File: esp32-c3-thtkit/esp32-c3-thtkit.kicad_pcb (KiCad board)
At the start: 4 copper layers, 17.9 x 24.5 mm, 28 parts, among them J1 PIN_GROUP_1, J2 PIN_GROUP_3, J3 PIN_GROUP_2, J4 UART, U1 MIC5219-3.3YM5, U2 ESP32-C3, Y1 32.768kHz ±20ppm CL12.5pF, Y2 40MHz ±10ppm CL8pF

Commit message: Draw pin layout on user layer
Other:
- board text added: "BOOT"
- board text added: "ESP32-C3-THTKIT"
- board text added: "GND"
- board text added: "GPIO10"
- board text added: "GPIO18"
- board text added: "GPIO19"
- board text added: "GPIO2"
- board text added: "GPIO3"
- board text added: "GPIO8"
- board text added: "MTCK"
- board text added: "MTDI"
- board text added: "MTDO"
- board text added: "MTMS"
- board text added: "RESET"
- board text added: "RX"
- board text added: "SPICLK"
- board text added: "SPICSO"
- board text added: "SPID"
- board text added: "SPIHD"
- board text added: "SPIQ"
- board text added: "SPIWP"
- board text added: "TX"
- board text added: "VIN"
- board text removed: "ESP32-C2-THTKIT"

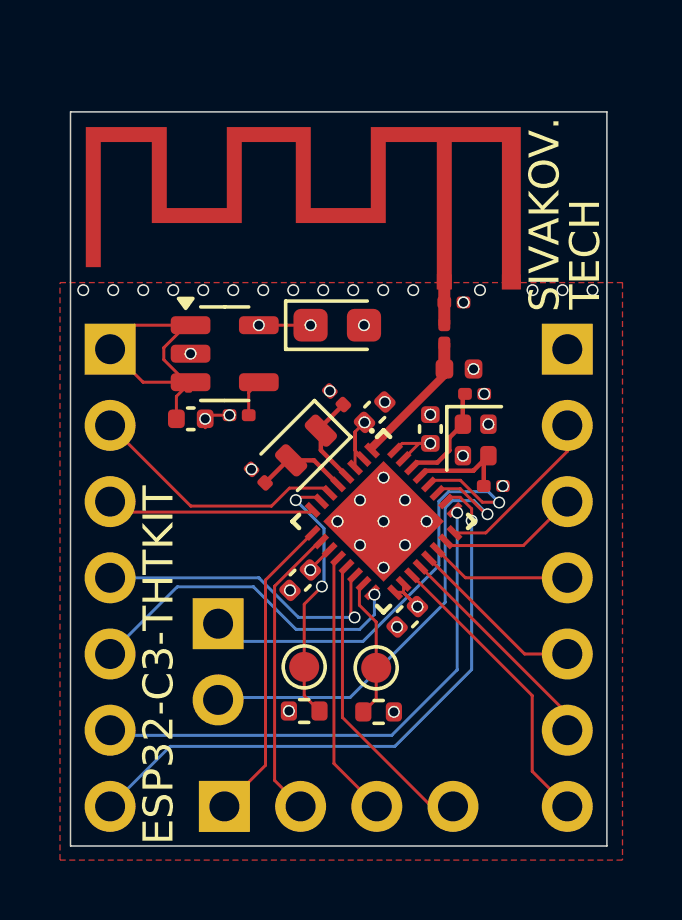
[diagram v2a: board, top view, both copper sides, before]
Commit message: Make devkits cheaper by using 0402 components instead of 0201
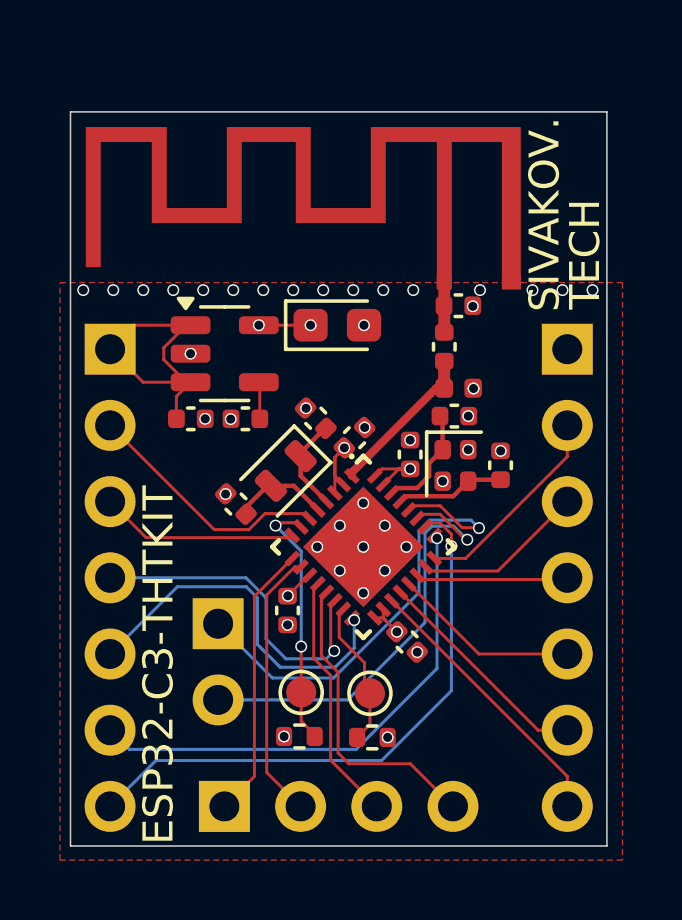
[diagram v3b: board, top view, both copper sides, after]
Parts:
- C10, C13: value 6p 6.3V C0G -> 15p 6.3V C0G; footprint Capacitor_SMD:C_0201_0603Metric -> Capacitor_SMD:C_0402_1005Metric
- C11, C12: value 15p 6.3V C0G -> 25p 6.3V C0G; footprint Capacitor_SMD:C_0201_0603Metric -> Capacitor_SMD:C_0402_1005Metric
- C2, C7, C9: footprint Capacitor_SMD:C_0201_0603Metric -> Capacitor_SMD:C_0402_1005Metric
- moved C12 1.19 mm to (189.6, 114.4)
- moved C5 1.09 mm to (191.3, 117.9), turned to 90 degrees
- moved C4 1.08 mm to (193.6, 112.2)
- moved C8 1.08 mm to (195.4, 112.7)
- moved U2 1.08 mm to (193.9, 115.8)
- moved Y2 1.08 mm to (196.9, 113.1)
- moved Y1 1.08 mm to (191.3, 113.3)
- moved C10 1.00 mm to (196.9, 111.5)
- moved C11 0.97 mm to (192.3, 111.5)
- moved R1 0.88 mm to (194.2, 122.2)
- moved TP1 0.88 mm to (194.1, 120.7)
- moved R2 0.86 mm to (191.7, 122.1)
- moved TP2 0.86 mm to (191.8, 120.7)
- moved C6 0.84 mm to (195.3, 119.0), turned to 135 degrees
- moved C13 0.73 mm to (198.4, 113.1), turned to -90 degrees
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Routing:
- net /GPIO18: track 17.8 -> 16.6 mm
- net /SPIQ: track 5.75 -> 6.88 mm
- net /MTMS: track 10.3 -> 9.21 mm
- net /GPIO19: track 20.4 -> 19.3 mm
- net /GPIO10: track 11.2 -> 12.3 mm
- net /U0RXD: track 15.9 -> 14.8 mm
- net /GPIO8: track 10.2 -> 11.3 mm
- net /SPID: track 4.71 -> 5.73 mm
- net /MTDO: track 9.99 -> 10.9 mm
- net GND: track 0.86 -> 0.00 mm
- net /MTDI: track 9.87 -> 9.04 mm
- net /RF: track 4.47 -> 5.27 mm
- net /U0TXD: track 15.8 -> 16.5 mm
- net /SPIHD: track 9.85 -> 9.27 mm
- net /MTCK: track 8.92 -> 8.34 mm
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
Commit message: Change microcontroller package from 4x4 to 5x5
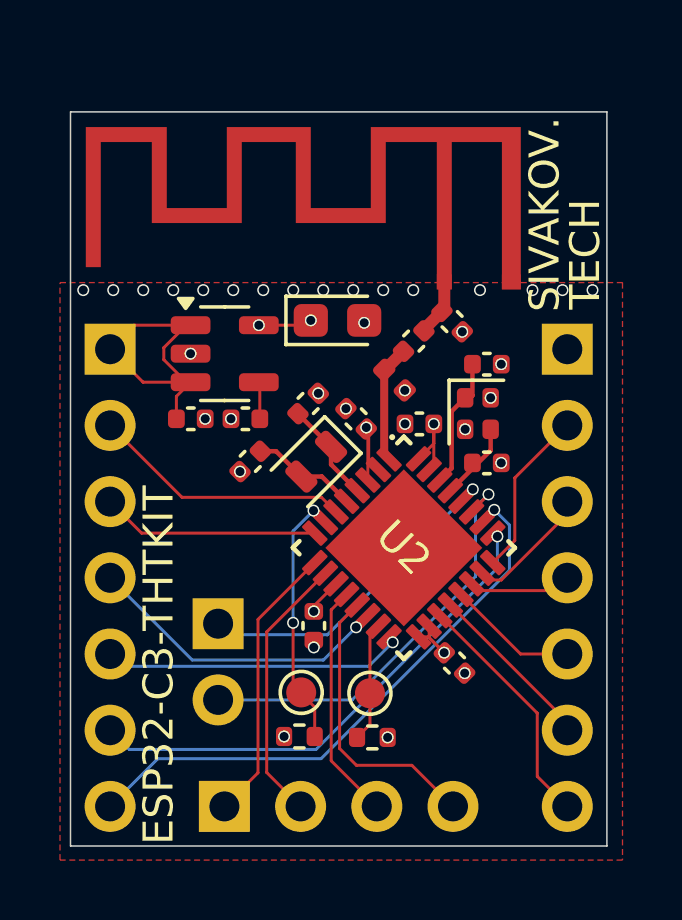
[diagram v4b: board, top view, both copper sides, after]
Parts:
- U2: footprint PCM_SKC_MCU_Espressif:TQFN_32_1EP_4x4mm_P0.4mm_EP2.4x2.4mm_Compact -> PCM_SKC_MCU_Espressif:VFQFN_32_1EP_5x5mm_P0.5mm_EP3.2x3.2mm_Compact
- moved L1 2.16 mm to (194.9, 110.2), turned to -45 degrees
- moved C10 2.04 mm to (198.0, 109.7)
- moved Y2 1.88 mm to (197.7, 111.4)
- moved C6 1.73 mm to (196.9, 119.7)
- moved C12 1.50 mm to (190.1, 113.0), turned to 45 degrees
- moved U2 1.35 mm to (195.2, 115.8)
- moved C8 1.07 mm to (195.7, 111.7), turned to 0 degrees
- moved Y1 1.06 mm to (192.3, 113.0)
- moved C7 1.04 mm to (195.5, 109.0), turned to -135 degrees
- moved C5 1.01 mm to (192.2, 118.4)
- moved C4 0.63 mm to (193.6, 111.5), turned to -45 degrees
- moved C9 0.57 mm to (196.8, 108.3), turned to 135 degrees
- moved C11 0.55 mm to (192.0, 111.0), turned to -135 degrees
- moved C13 0.46 mm to (198.0, 113.0), turned to 180 degrees
- moved C3 0.16 mm to (193.0, 108.3)
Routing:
- net /U0TXD: track 16.5 -> 11.2 mm
- net /GPIO10: track 12.3 -> 10.2 mm
- net /SPICS0: track 6.25 -> 4.37 mm
- net +3.3V: track 9.66 -> 11.5 mm
- net /SPIWP: track 8.02 -> 6.34 mm
- net /SPICLK: track 5.08 -> 3.46 mm
- net /SPID: track 5.73 -> 4.26 mm
- net /RF: track 5.27 -> 3.96 mm
- net /SPIQ: track 6.88 -> 5.60 mm
- net /XTAL_N: track 3.86 -> 2.60 mm
- net /SPIHD: track 9.27 -> 8.12 mm
- net /GPIO8: track 11.3 -> 10.3 mm
- net /U0RXD: track 14.8 -> 14.1 mm
- net /XTAL_P: track 3.55 -> 4.24 mm
- net /BOOT: track 4.93 -> 4.26 mm
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
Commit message: Unify schemas and fix esp32-c3 footprint
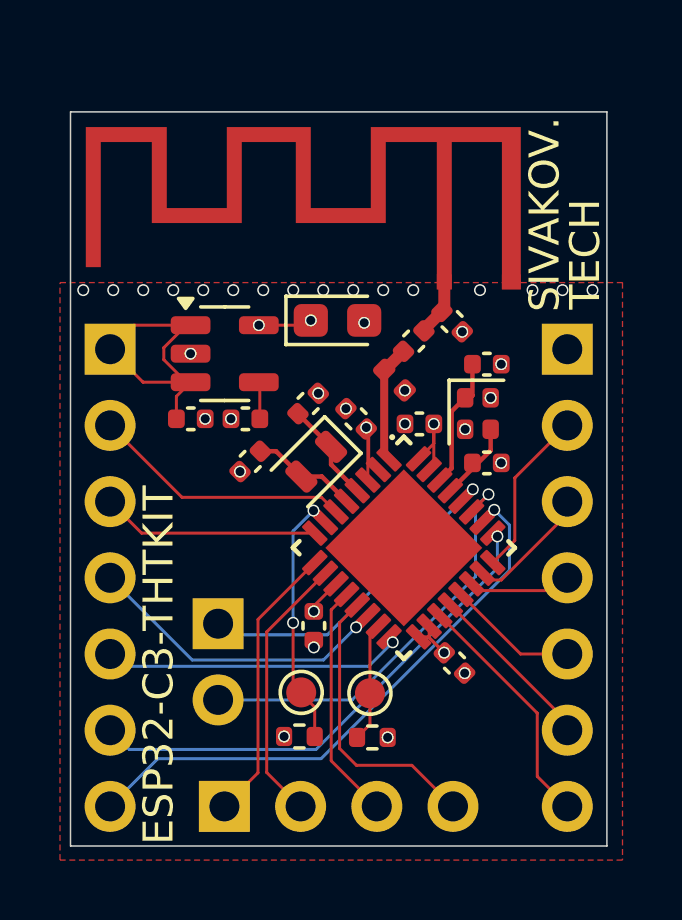
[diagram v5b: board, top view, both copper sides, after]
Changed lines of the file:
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@@
 			(unlocked yes)
 			(layer "F.SilkS")
+			(hide yes)
 			(effects
 				(font
@@
 			(unlocked yes)
 			(layer "F.Fab")
+			(hide yes)
 			(effects
 				(font
@@
 			)
 		)
-		(property "Datasheet" "https://cdn.jsdelivr.net/gh/sivakov512/kicad-library@master/datasheets/MCU/Espressif/Espressif_ESP32-C3.pdf"
+		(property "Datasheet" ""
 			(at -0.3 -6.699999 315)
 			(layer "F.Fab")
@@
 			)
 		)
-		(property "Description" "2.4 GHz Wi-Fi + BLE 5 LE SoC, 32-bit RISC-V MCU, 22 GPIO, QFN32"
+		(property "Description" ""
 			(at -0.3 -6.699999 315)
 			(layer "F.Fab")
@@
 		(sheetfile "esp32-c3-thtkit.kicad_sch")
 		(attr smd)
-		(fp_poly
-			(pts
-				(xy -1.9 -1.9) (xy 1.9 -1.9) (xy 1.9 1.9) (xy -1.9 1.9)
-			)
-			(stroke
-				(width 0.01)
-				(type solid)
-			)
-			(fill yes)
-			(layer "F.Mask")
-		)
 		(fp_line
 			(start -2.62 2.61)
@@
 			(at -2.445 -1.75 315)
 			(size 0.92 0.34)
-			(layers "F.Cu" "F.Paste")
+			(layers "F.Cu" "F.Mask" "F.Paste")
 			(roundrect_rratio 0.125)
 			(net 6 "/RF")
@@
 			(at -2.445001 -1.25 315)
 			(size 0.92 0.34)
-			(layers "F.Cu" "F.Paste")
+			(layers "F.Cu" "F.Mask" "F.Paste")
 			(roundrect_rratio 0.125)
 			(net 5 "+3.3V")
@@
 			(at -2.445 -0.75 315)
 			(size 0.92 0.34)
-			(layers "F.Cu" "F.Paste")
+			(layers "F.Cu" "F.Mask" "F.Paste")
 			(roundrect_rratio 0.125)
 			(net 5 "+3.3V")
@@
 			(at -2.445 -0.25 315)
 			(size 0.92 0.34)
-			(layers "F.Cu" "F.Paste")
+			(layers "F.Cu" "F.Mask" "F.Paste")
 			(roundrect_rratio 0.125)
 			(net 8 "/XTAL_32K_P")
@@
 			(at -2.445 0.25 315)
 			(size 0.92 0.34)
-			(layers "F.Cu" "F.Paste")
+			(layers "F.Cu" "F.Mask" "F.Paste")
 			(roundrect_rratio 0.125)
 			(net 9 "/XTAL_32K_N")
@@
 			(at -2.445 0.75 315)
 			(size 0.92 0.34)
-			(layers "F.Cu" "F.Paste")
+			(layers "F.Cu" "F.Mask" "F.Paste")
 			(roundrect_rratio 0.125)
 			(net 30 "/GPIO2")
@@
 			(at -2.445001 1.25 315)
 			(size 0.92 0.34)
-			(layers "F.Cu" "F.Paste")
+			(layers "F.Cu" "F.Mask" "F.Paste")
 			(roundrect_rratio 0.125)
 			(net 18 "/RESET")
@@
 			(at -2.445 1.75 315)
 			(size 0.92 0.34)
-			(layers "F.Cu" "F.Paste")
+			(layers "F.Cu" "F.Mask" "F.Paste")
 			(roundrect_rratio 0.125)
 			(net 22 "/GPIO3")
@@
 			(at -1.75 2.445 315)
 			(size 0.34 0.92)
-			(layers "F.Cu" "F.Paste")
+			(layers "F.Cu" "F.Mask" "F.Paste")
 			(roundrect_rratio 0.125)
 			(net 14 "/MTMS")
@@
 			(at -1.25 2.445001 315)
 			(size 0.34 0.92)
-			(layers "F.Cu" "F.Paste")
+			(layers "F.Cu" "F.Mask" "F.Paste")
 			(roundrect_rratio 0.125)
 			(net 13 "/MTDI")
@@
 			(at -0.75 2.445 315)
 			(size 0.34 0.92)
-			(layers "F.Cu" "F.Paste")
+			(layers "F.Cu" "F.Mask" "F.Paste")
 			(roundrect_rratio 0.125)
 			(net 5 "+3.3V")
@@
 			(at -0.25 2.445 315)
 			(size 0.34 0.92)
-			(layers "F.Cu" "F.Paste")
+			(layers "F.Cu" "F.Mask" "F.Paste")
 			(roundrect_rratio 0.125)
 			(net 12 "/MTCK")
@@
 			(at 0.25 2.445 315)
 			(size 0.34 0.92)
-			(layers "F.Cu" "F.Paste")
+			(layers "F.Cu" "F.Mask" "F.Paste")
 			(roundrect_rratio 0.125)
 			(net 11 "/MTDO")
@@
 			(at 0.75 2.445 315)
 			(size 0.34 0.92)
-			(layers "F.Cu" "F.Paste")
+			(layers "F.Cu" "F.Mask" "F.Paste")
 			(roundrect_rratio 0.125)
 			(net 19 "/GPIO8")
@@
 			(at 1.25 2.445001 315)
 			(size 0.34 0.92)
-			(layers "F.Cu" "F.Paste")
+			(layers "F.Cu" "F.Mask" "F.Paste")
 			(roundrect_rratio 0.125)
 			(net 17 "/BOOT")
@@
 			(at 1.75 2.445 315)
 			(size 0.34 0.92)
-			(layers "F.Cu" "F.Paste")
+			(layers "F.Cu" "F.Mask" "F.Paste")
 			(roundrect_rratio 0.125)
 			(net 24 "/GPIO10")
@@
 			(at 2.445 1.75 315)
 			(size 0.92 0.34)
-			(layers "F.Cu" "F.Paste")
+			(layers "F.Cu" "F.Mask" "F.Paste")
 			(roundrect_rratio 0.125)
 			(net 5 "+3.3V")
@@
 			(at 2.445001 1.25 315)
 			(size 0.92 0.34)
-			(layers "F.Cu" "F.Paste")
+			(layers "F.Cu" "F.Mask" "F.Paste")
 			(roundrect_rratio 0.125)
 			(net 5 "+3.3V")
@@
 			(at 2.445 0.75 315)
 			(size 0.92 0.34)
-			(layers "F.Cu" "F.Paste")
+			(layers "F.Cu" "F.Mask" "F.Paste")
 			(roundrect_rratio 0.125)
 			(net 25 "/SPIHD")
@@
 			(at 2.445 0.25 315)
 			(size 0.92 0.34)
-			(layers "F.Cu" "F.Paste")
+			(layers "F.Cu" "F.Mask" "F.Paste")
 			(roundrect_rratio 0.125)
 			(net 28 "/SPIWP")
@@
 			(at 2.445 -0.25 315)
 			(size 0.92 0.34)
-			(layers "F.Cu" "F.Paste")
+			(layers "F.Cu" "F.Mask" "F.Paste")
 			(roundrect_rratio 0.125)
 			(net 27 "/SPICS0")
@@
 			(at 2.445 -0.75 315)
 			(size 0.92 0.34)
-			(layers "F.Cu" "F.Paste")
+			(layers "F.Cu" "F.Mask" "F.Paste")
 			(roundrect_rratio 0.125)
 			(net 20 "/SPICLK")
@@
 			(at 2.445001 -1.25 315)
 			(size 0.92 0.34)
-			(layers "F.Cu" "F.Paste")
+			(layers "F.Cu" "F.Mask" "F.Paste")
 			(roundrect_rratio 0.125)
 			(net 23 "/SPID")
@@
 			(at 2.445 -1.75 315)
 			(size 0.92 0.34)
-			(layers "F.Cu" "F.Paste")
+			(layers "F.Cu" "F.Mask" "F.Paste")
 			(roundrect_rratio 0.125)
 			(net 21 "/SPIQ")
@@
 			(at 1.75 -2.445 315)
 			(size 0.34 0.92)
-			(layers "F.Cu" "F.Paste")
+			(layers "F.Cu" "F.Mask" "F.Paste")
 			(roundrect_rratio 0.125)
 			(net 29 "/GPIO18")
@@
 			(at 1.25 -2.445001 315)
 			(size 0.34 0.92)
-			(layers "F.Cu" "F.Paste")
+			(layers "F.Cu" "F.Mask" "F.Paste")
 			(roundrect_rratio 0.125)
 			(net 26 "/GPIO19")
@@
 			(at 0.75 -2.445 315)
 			(size 0.34 0.92)
-			(layers "F.Cu" "F.Paste")
+			(layers "F.Cu" "F.Mask" "F.Paste")
 			(roundrect_rratio 0.125)
 			(net 15 "/U0RXD")
@@
 			(at 0.25 -2.445 315)
 			(size 0.34 0.92)
-			(layers "F.Cu" "F.Paste")
+			(layers "F.Cu" "F.Mask" "F.Paste")
 			(roundrect_rratio 0.125)
 			(net 16 "/U0TXD")
@@
 			(at -0.25 -2.445 315)
 			(size 0.34 0.92)
-			(layers "F.Cu" "F.Paste")
+			(layers "F.Cu" "F.Mask" "F.Paste")
 			(roundrect_rratio 0.125)
 			(net 10 "/XTAL_N")
@@
 			(at -0.75 -2.445 315)
 			(size 0.34 0.92)
-			(layers "F.Cu" "F.Paste")
+			(layers "F.Cu" "F.Mask" "F.Paste")
 			(roundrect_rratio 0.125)
 			(net 7 "/XTAL_P")
@@
 			(at -1.25 -2.445001 315)
 			(size 0.34 0.92)
-			(layers "F.Cu" "F.Paste")
+			(layers "F.Cu" "F.Mask" "F.Paste")
 			(roundrect_rratio 0.125)
 			(net 5 "+3.3V")
@@
 			(at -1.75 -2.445 315)
 			(size 0.34 0.92)
-			(layers "F.Cu" "F.Paste")
+			(layers "F.Cu" "F.Mask" "F.Paste")
 			(roundrect_rratio 0.125)
 			(net 5 "+3.3V")
@@
 			(at 0 0 315)
 			(size 3.7 3.7)
-			(layers "F.Cu")
+			(layers "F.Cu" "F.Mask" "F.Paste")
 			(net 2 "GND")
 			(pinfunction "GND")
